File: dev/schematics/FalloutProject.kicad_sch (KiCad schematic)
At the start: 44 parts

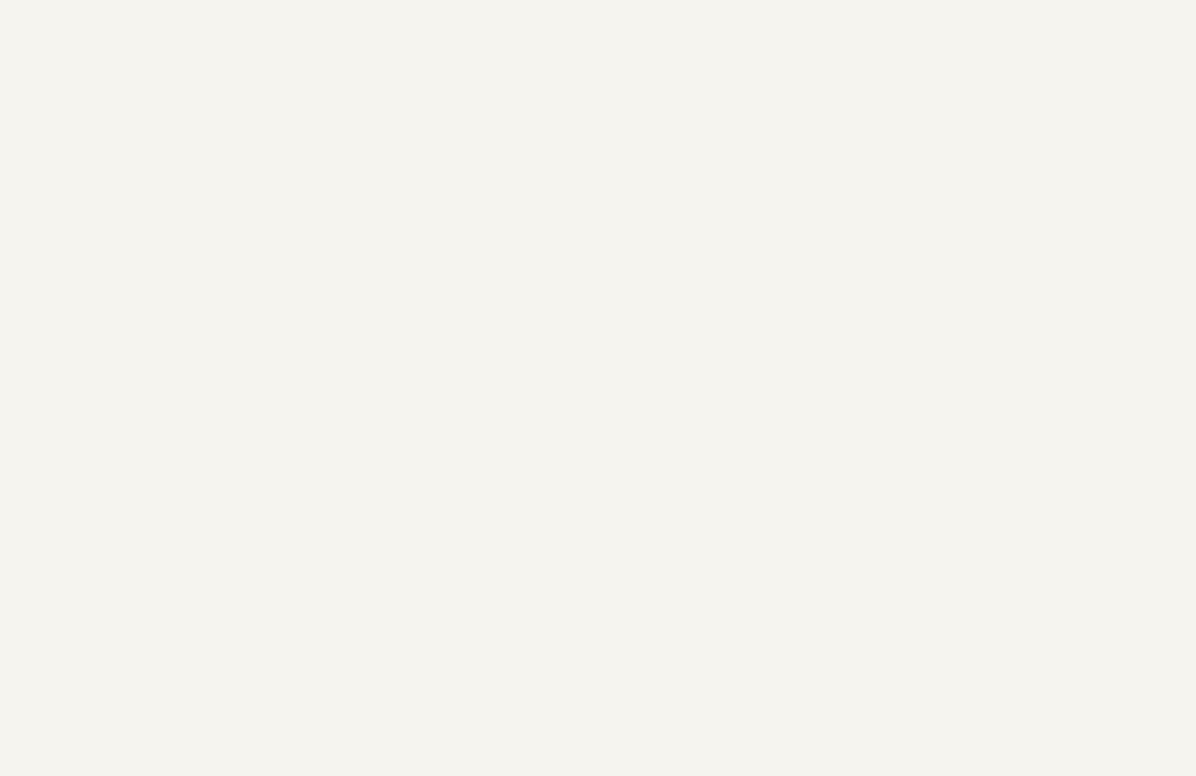
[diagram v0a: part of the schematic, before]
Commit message: Change MOSFETs to NPN
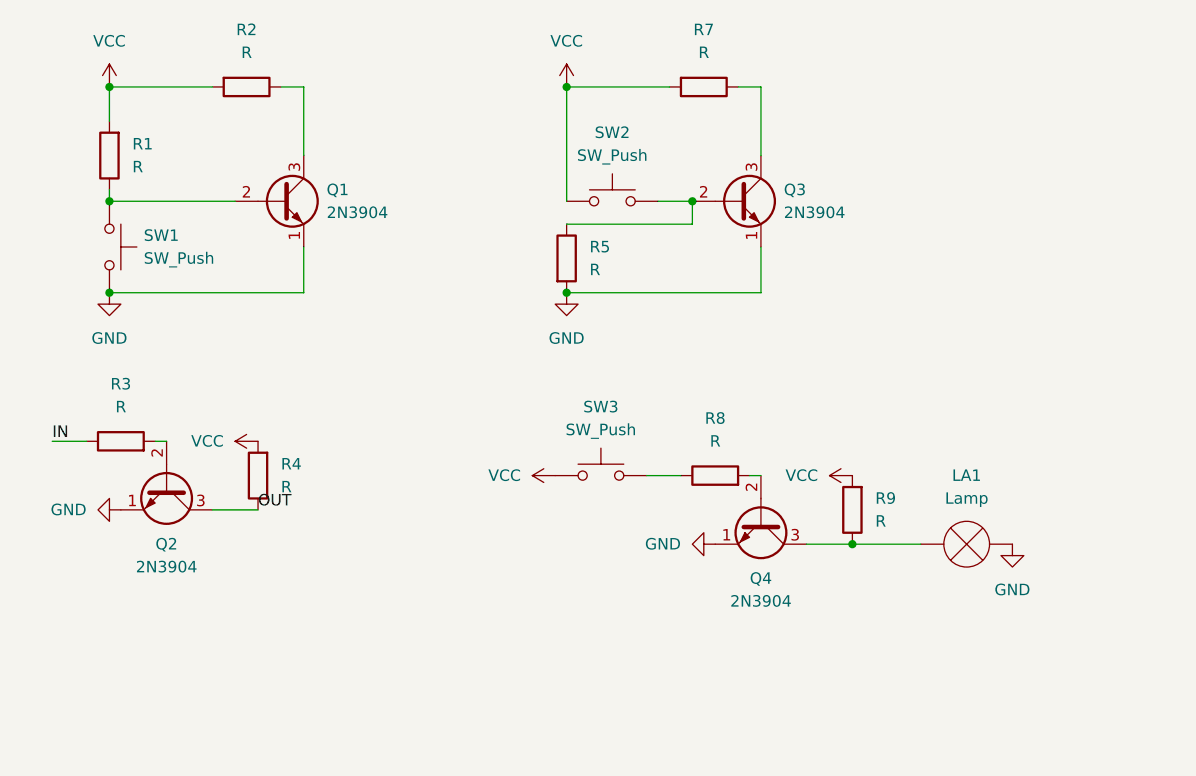
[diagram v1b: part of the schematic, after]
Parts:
- added LA1: Lamp, symbol Device:Lamp
- added Q1, Q2, Q3, Q4: 2N3904, Package_TO_SOT_THT:TO-92_Inline, symbol Transistor_BJT:2N3904
- added R1, R2, R3, R4, R5, R7, R8, R9: R, symbol Device:R
- added SW1, SW2, SW3: SW_Push, symbol Switch:SW_Push
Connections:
- net IN: now also R3.1
- new net: LA1.2 (+), Q4.3 (C), R9.1
- new net: Q3.2 (B), R5.1, SW2.2
- new net: Q2.2 (B), R3.2
- new net: Q1.2 (B), R1.1, SW1.1
- new net: Q3.3 (C), R7.1
- new net: R8.1, SW3.2
- new net: Q4.2 (B), R8.2
- new net: Q1.3 (C), R2.1
- new net GND: LA1.1 (-), Q1.1 (E), Q2.1 (E), Q3.1 (E), Q4.1 (E), R5.2, SW1.2
- new net OUT: Q2.3 (C), R4.1
- new net VCC: R1.2, R2.2, R4.2, R7.2, R9.2, SW2.1, SW3.1
